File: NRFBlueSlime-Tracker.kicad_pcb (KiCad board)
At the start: 4 copper layers, 38 x 20 mm, 61 parts, among them J1 GT-USB-7010ASV, Q1 NTS2101PT1G, SW1 TS-1088-AR02016, U1 ICM-45686, U2 E73-2G4M08S1C, U3 LIS2MDL, U4 EA8103DHR, U5 TP4057-42-SOT26-R, X1 S2D32.768KB20F30T, Y1 Q13FC13500004

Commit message: sihashkdasfhjkads
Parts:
- removed D8: 1N5819WS, Diode_SMD:D_SOD-323
- removed Q1: NTS2101PT1G, Package_TO_SOT_SMD:SOT-323_SC-70
- added C18: 10u, Capacitor_SMD:C_0603_1608Metric, F.Cu at (52.6, 47.2)
- added C19: 100n, Capacitor_SMD:C_0402_1005Metric, F.Cu at (42.3, 37.2)
- added C20: 10u, Capacitor_SMD:C_0603_1608Metric, F.Cu at (56.6, 39.7)
- added C21: 100n, Capacitor_SMD:C_0402_1005Metric, F.Cu at (42.3, 39.2)
- added C22: 10u, Capacitor_SMD:C_0603_1608Metric, F.Cu at (56.6, 42.2)
- added C23: 100n, Capacitor_SMD:C_0402_1005Metric, F.Cu at (45.2, 29.3)
- added C24: 220n, Capacitor_SMD:C_0402_1005Metric, F.Cu at (45.2, 31.3)
- added C25: 220n, Capacitor_SMD:C_0402_1005Metric, F.Cu at (45.2, 33.3)
- added L2: 2.2u, Inductor_SMD:L_1210_3225Metric, F.Cu at (40.8, 42.3)
- added Y2: XL7EL89CKI-111YLC-32M, Crystal:Crystal_SMD_2016-4Pin_2.0x1.6mm, F.Cu at (43.8, 54.3)
- C1: value 10u -> 100p; footprint Capacitor_SMD:C_0603_1608Metric -> Capacitor_SMD:C_0402_1005Metric
- C10, C2: value 100n -> 1u; footprint Capacitor_SMD:C_0402_1005Metric -> Capacitor_SMD:C_0603_1608Metric
- C11, C6: value 220n -> 100n
- C12: value 10u -> 1u
- C13: value 10u -> 100n; footprint Capacitor_SMD:C_0603_1608Metric -> Capacitor_SMD:C_0402_1005Metric
- C14: value 1u -> 10u
- C16, C17: value 22p -> 4.7u; footprint Capacitor_SMD:C_0402_1005Metric -> Capacitor_SMD:C_0603_1608Metric
- C3: value 100n -> 100p
- C4: value 10u -> 15p; footprint Capacitor_SMD:C_0603_1608Metric -> Capacitor_SMD:C_0402_1005Metric
- C5: value 100n -> 15p
- C7: value 1u -> 0.8p; footprint Capacitor_SMD:C_0603_1608Metric -> Capacitor_SMD:C_0402_1005Metric
- C8: value 100n -> 6.8p
- C9: value 1u -> 6.8p; footprint Capacitor_SMD:C_0603_1608Metric -> Capacitor_SMD:C_0402_1005Metric
- L1: value 2.2u -> 4.7n; footprint Inductor_SMD:L_1210_3225Metric -> Inductor_SMD:L_0402_1005Metric
- R1, R2: value 5.1k -> 27
- R10: value 100k -> 51k
- R11: value 51k -> 10k; footprint Resistor_SMD:R_0603_1608Metric -> Resistor_SMD:R_0402_1005Metric
- R3: value 27 -> 1k
- R4: value 27 -> 5.1k
- R5: value 1k -> 5.1k
- R8: value 100k -> 10k; footprint Resistor_SMD:R_0603_1608Metric -> Resistor_SMD:R_0402_1005Metric
- R9: value 1k -> 100k; footprint Resistor_SMD:R_0402_1005Metric -> Resistor_SMD:R_0603_1608Metric
- TP1, TP2, TP3, TP4, TP5, TP6: moved to F.Cu
- U1: value ICM-45686 -> nRF52840; footprint 42688:PQFN50P300X250X97-14N -> Package_DFN_QFN:Nordic_AQFN-73-1EP_7x7mm_P0.5mm
- U2: value E73-2G4M08S1C -> EA8103DHR; footprint nrf:E73-2G4M08S1C_nobottom -> nrfslime:DFN-6_L1.5-W1.5-P0.50-BL-EP1.0
- U3: value LIS2MDL -> BQ24075RGT; footprint Package_LGA:LGA-12_2x2mm_P0.5mm -> Package_DFN_QFN:VQFN-16-1EP_3x3mm_P0.5mm_EP1.6x1.6mm
- U4: value EA8103DHR -> ICM-45686; footprint nrfslime:DFN-6_L1.5-W1.5-P0.50-BL-EP1.0 -> 42688:PQFN50P300X250X97-14N
- U5: value TP4057-42-SOT26-R -> LIS2MDL; footprint Package_TO_SOT_SMD:SOT-23-6 -> Package_LGA:LGA-12_2x2mm_P0.5mm
- Y1: value Q13FC13500004 -> XKXGI-SUA-32.768K
- moved U5 45.7 mm to (40.0, 54.5), turned to 0 degrees
- moved C11 40.6 mm to (42.3, 33.3)
- moved U4 40.3 mm to (40.7, 50.5)
- moved D4 38.1 mm to (48.0, 56.7), turned to 0 degrees
- moved C13 37.1 mm to (42.3, 35.2)
- moved D7 35.7 mm to (50.7, 54.3), turned to 0 degrees
- moved C6 34.7 mm to (39.4, 37.2), turned to 0 degrees
- moved D6 34.4 mm to (50.7, 52.0), turned to 0 degrees
- moved C15 33.7 mm to (52.6, 39.7), turned to 0 degrees
- moved C14 33.7 mm to (48.6, 47.2), turned to 0 degrees
- moved C4 33.4 mm to (39.4, 33.3)
- moved D5 33.1 mm to (50.7, 49.6), turned to 0 degrees
- moved C12 33.1 mm to (48.6, 44.7), turned to 0 degrees
- moved C1 33.0 mm to (39.4, 29.3), turned to 0 degrees
- moved LED3 32.2 mm to (54.1, 54.9), turned to 0 degrees
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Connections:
- C1 pad 1: +3V3 -> GND
- C1 pad 2: GND -> Net-(U1-DEC4)
- C10 pad 1: +3V3 -> VBUS
- C11 pad 1: KEY -> VBUS
- C12 pad 1: VDC -> +3V3
- C14 pad 1: GND -> VDC
- C14 pad 2: VBUS -> GND
- C15 pad 1: +BATT -> +3V3
- C16 pad 1: Net-(U2-XL1) -> GND
- C16 pad 2: Net-(C16-Pad2) -> VBUS
- C17 pad 1: Net-(U2-XL2) -> GND
- C17 pad 2: Net-(C17-Pad2) -> Net-(LED2-A)
- C2 pad 1: +3V3 -> GND
- C2 pad 2: GND -> Net-(U1-DEC4)
- C3 pad 1: +3V3 -> GND
- C3 pad 2: GND -> Net-(U1-DEC3)
- C4 pad 1: +3V3 -> Net-(U1-XL1/P0.00)
- C4 pad 2: GND -> Net-(C4-Pad2)
- C5 pad 1: +3V3 -> Net-(U1-XL2/P0.01)
- C5 pad 2: GND -> Net-(C5-Pad2)
- C6 pad 1: Net-(U3-C1) -> GND
- C6 pad 2: GND -> Net-(U1-DEC1)
- C7 pad 1: VBUS -> GND
- C7 pad 2: GND -> Net-(U1-ANT)
- C8 pad 1: VBUS -> Net-(C8-Pad1)
- C8 pad 2: GND -> Net-(U1-XC1)
- C9 pad 1: +3V3 -> Net-(C9-Pad1)
- C9 pad 2: GND -> Net-(U1-XC2)
- D6 pad 1: ~{RST} -> DOCK
- D7 pad 1: DOCK -> ~{RST}
- L1 pad 1: Net-(U4-SW) -> unconnected-(L1-Pad1)
- L1 pad 2: +3V3 -> Net-(U1-ANT)
- R1 pad 1: Net-(J1-CC1) -> DN
- R1 pad 2: GND -> Net-(U1-D-)
- R10 pad 1: BATLVL -> ~{ADC_EN}
- R10 pad 2: +BATT -> BATLVL
- R11 pad 1: ~{ADC_EN} -> Net-(U3-ISET)
- R11 pad 2: BATLVL -> GND
- R12 pad 1: GND -> Net-(U3-TS)
- R12 pad 2: Net-(U5-PROG) -> GND
- R2 pad 1: Net-(J1-CC2) -> DP
- R2 pad 2: GND -> Net-(U1-D+)
- R3 pad 1: DN -> Net-(LED1-A)
- R3 pad 2: Net-(U2-D-) -> +3V3
- R4 pad 1: DP -> Net-(J1-CC1)
- R4 pad 2: Net-(U2-D+) -> GND
- R5 pad 1: Net-(LED1-A) -> Net-(J1-CC2)
- R5 pad 2: +3V3 -> GND
- R6 pad 2: Net-(U4-FB) -> Net-(U2-FB)
- R7 pad 1: Net-(U4-FB) -> Net-(U2-FB)
- R8 pad 1: GND -> Net-(LED2-A)
- R8 pad 2: VBUS -> VDC
- R9 pad 1: Net-(LED2-A) -> BATLVL
- R9 pad 2: VBUS -> +BATT
- U2 pad 1: MOSI -> Net-(U2-SW)
- U2 pad 2: MISO -> VDC
- U2 pad 3: ~{ADC_EN} -> Net-(U2-FB)
- U2 pad 4: OSC_EN -> GND
- U2 pad 5: GND -> unconnected-(U2-NC-Pad5)
- U2 pad 6: ~{CS}_IMU -> VDC
- U2 pad 7: DOCK -> GND
- U3 pad 1: SCLK -> Net-(U3-TS)
- U3 pad 10: +3V3 -> VDC
- U3 pad 11: unconnected-(U3-NC-Pad11) -> VDC
- U3 pad 2: unconnected-(U3-NC-Pad2) -> +BATT
- U3 pad 3: ~{CS}_MAG -> +BATT
- U3 pad 4: MOSI -> GND
- U3 pad 5: Net-(U3-C1) -> GND
- U3 pad 6: GND -> VDC
- U3 pad 7: MISO -> Net-(LED2-K)
- U3 pad 9: +3V3 -> Net-(LED3-K)
- U4 pad 1: Net-(U4-SW) -> MISO
- U4 pad 2: VDC -> GND
- U4 pad 3: Net-(U4-FB) -> GND
- U4 pad 4: GND -> INT
- U4 pad 5: unconnected-(U4-NC-Pad5) -> +3V3
- U4 pad 6: VDC -> GND
- U5 pad 1: Net-(LED2-K) -> SCLK
- U5 pad 2: GND -> unconnected-(U5-NC-Pad2)
- U5 pad 3: +BATT -> ~{CS}_MAG
- U5 pad 4: VBUS -> MOSI
- U5 pad 5: Net-(LED3-K) -> Net-(U5-C1)
- U5 pad 6: Net-(U5-PROG) -> GND
- Y1 pad 1: Net-(C16-Pad2) -> Net-(C4-Pad2)
- Y1 pad 2: Net-(C17-Pad2) -> Net-(C5-Pad2)
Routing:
- net DOCK: track 41.8 -> 0.00 mm, vias 2 -> 0
- net VBUS: track 41.1 -> 0.00 mm, vias 4 -> 0
- net GND: track 39.8 -> 0.00 mm, vias 14 -> 0
- net BATLVL: track 35.2 -> 0.00 mm, vias 4 -> 0
- net ~{CS}_MAG: track 35.0 -> 0.00 mm, vias 2 -> 0
- net SWC: track 33.9 -> 0.00 mm, vias 2 -> 0
- net ~{RST}: track 31.7 -> 0.00 mm, vias 3 -> 0
- net MISO: track 30.5 -> 0.00 mm, vias 3 -> 0
- net ~{ADC_EN}: track 30.1 -> 0.00 mm, vias 2 -> 0
- net +3V3: track 26.7 -> 0.00 mm, vias 9 -> 0
- net MOSI: track 26.2 -> 0.00 mm, vias 3 -> 0
- net SWD: track 25.8 -> 0.00 mm, vias 2 -> 0
- net KEY: track 25.6 -> 0.00 mm, vias 3 -> 0
- net SCLK: track 24.1 -> 0.00 mm, vias 4 -> 0
- net ~{CS}_IMU: track 23.7 -> 0.00 mm, vias 3 -> 0
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- removed copper zone on In2.Cu, net +3V3
- removed copper zone on B.Cu, net GND
- removed copper zone on F.Cu, net GND
- removed copper zone on In1.Cu, net GND
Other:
- board outline removed
- board text removed: "+ -"

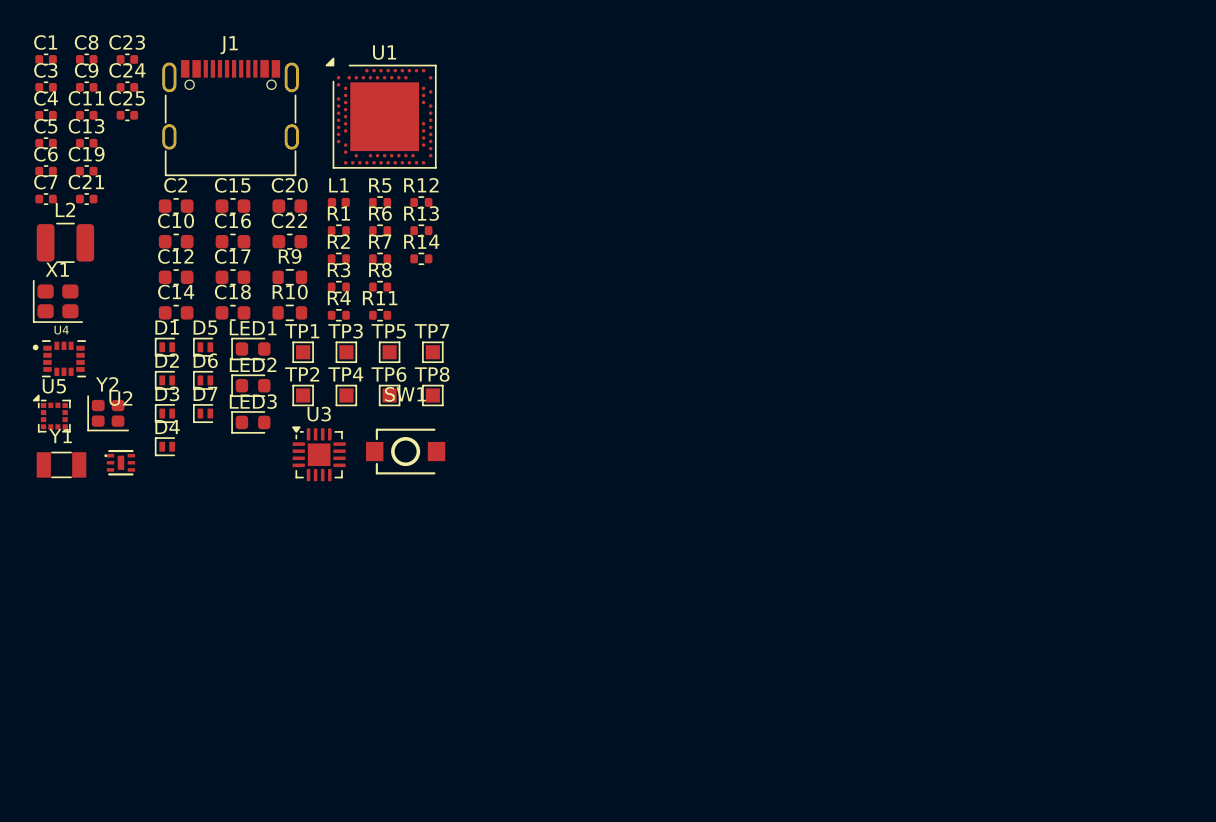
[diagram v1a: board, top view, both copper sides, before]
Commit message: place components
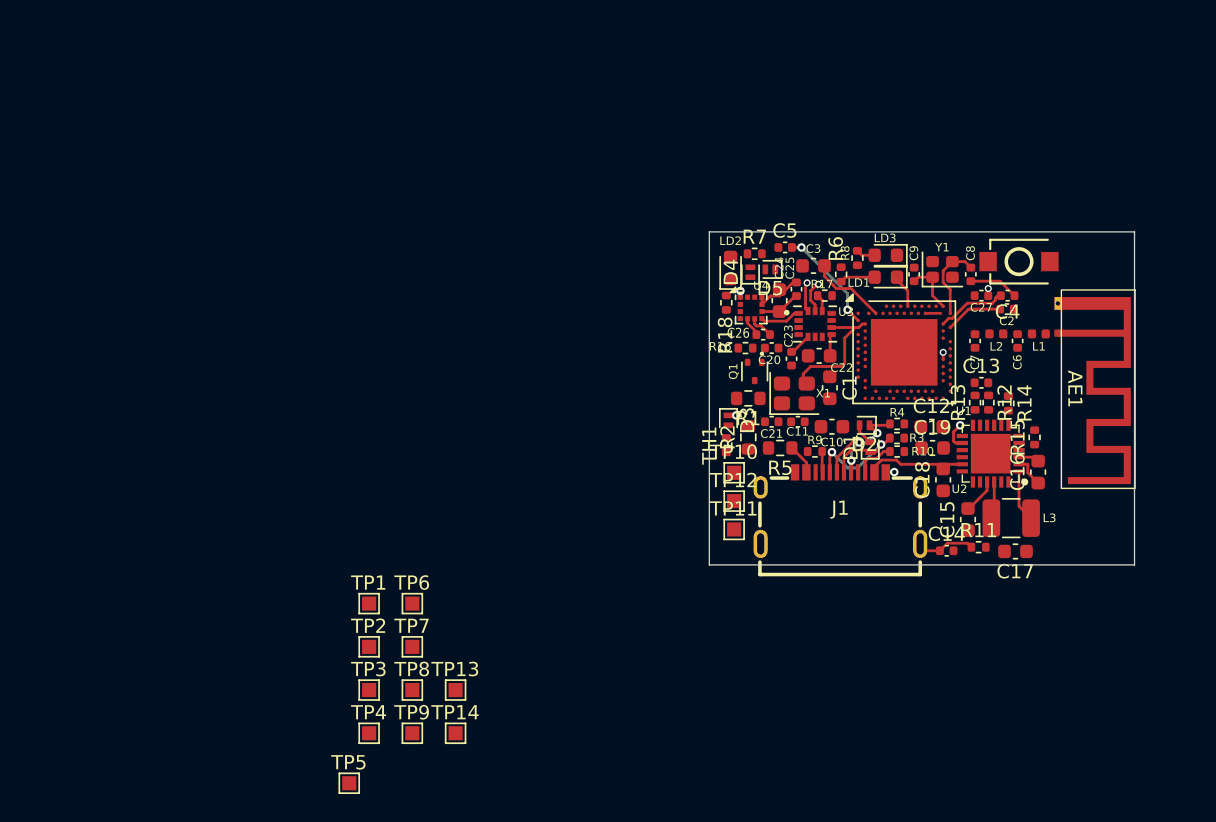
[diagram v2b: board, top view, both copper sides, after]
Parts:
- removed D6, D7: PESD5V0X1UB, Diode_SMD:D_SOD-882
- removed LED1: XL-1608UBC-04, LED_SMD:LED_0603_1608Metric
- removed LED2: XL-1608SURC-06, LED_SMD:LED_0603_1608Metric
- removed LED3: XL-1608UGC-06, LED_SMD:LED_0603_1608Metric
- removed U5: LIS2MDL, Package_LGA:LGA-12_2x2mm_P0.5mm
- removed Y2: XL7EL89CKI-111YLC-32M, Crystal:Crystal_SMD_2016-4Pin_2.0x1.6mm
- added AE1: Antenna_Shield, nrfslime:MIFA_BLE_ANT, F.Cu at (111.1, 48.6)
- added C26: 220n, Capacitor_SMD:C_0402_1005Metric, F.Cu at (90.0, 48.8)
- added C27: 220n, Capacitor_SMD:C_0402_1005Metric, F.Cu at (105.5, 46.0)
- added L3: 2.2u, Inductor_SMD:L_1210_3225Metric, F.Cu at (107.5, 61.7)
- added LD1: XL-1608UBC-04, LED_SMD:LED_0603_1608Metric, F.Cu at (98.7, 44.7)
- added LD2: XL-1608SURC-06, LED_SMD:LED_0603_1608Metric, F.Cu at (87.8, 44.0)
- added LD3: XL-1608UGC-06, LED_SMD:LED_0603_1608Metric, F.Cu at (98.7, 43.1)
- added Q1: YFW2301T, Package_TO_SOT_SMD:SOT-523, F.Cu at (89.5, 51.4)
- added R15: 470k, Resistor_SMD:R_0402_1005Metric, F.Cu at (109.2, 56.0)
- added R16: 470k, Resistor_SMD:R_0402_1005Metric, F.Cu at (88.8, 49.7)
- added R17: 470k, Resistor_SMD:R_0402_1005Metric, F.Cu at (94.4, 46.0)
- added R18: 470k, Resistor_SMD:R_0402_1005Metric, F.Cu at (87.5, 46.5)
- added TH1: HNTC0402-103F3380FB, Resistor_SMD:R_0402_1005Metric, F.Cu at (87.5, 56.5)
- added TP10: TestPoint, TestPoint:TestPoint_Pad_1.0x1.0mm, F.Cu at (88.0, 58.5)
- added TP11: TestPoint, TestPoint:TestPoint_Pad_1.0x1.0mm, F.Cu at (88.0, 62.5)
- added TP12: TestPoint, TestPoint:TestPoint_Pad_1.0x1.0mm, F.Cu at (88.0, 60.5)
- added TP13: TestPoint, TestPoint:TestPoint_Pad_1.0x1.0mm, F.Cu at (68.3, 73.8)
- added TP14: TestPoint, TestPoint:TestPoint_Pad_1.0x1.0mm, F.Cu at (68.3, 76.9)
- added TP9: TestPoint, TestPoint:TestPoint_Pad_1.0x1.0mm, F.Cu at (65.3, 76.9)
- C1: value 100p -> 4.7u; footprint Capacitor_SMD:C_0402_1005Metric -> Capacitor_SMD:C_0603_1608Metric
- C10, C12: value 1u -> 4.7u
- C14: value 10u -> 100n; footprint Capacitor_SMD:C_0603_1608Metric -> Capacitor_SMD:C_0402_1005Metric
- C16, C17: value 4.7u -> 10u
- C18: value 10u -> 2.2u
- C19: value 100n -> 1u; footprint Capacitor_SMD:C_0402_1005Metric -> Capacitor_SMD:C_0603_1608Metric
- C2: value 1u -> 100p; footprint Capacitor_SMD:C_0603_1608Metric -> Capacitor_SMD:C_0402_1005Metric
- C20: value 10u -> 1n; footprint Capacitor_SMD:C_0603_1608Metric -> Capacitor_SMD:C_0402_1005Metric
- C24: value 220n -> 10u; footprint Capacitor_SMD:C_0402_1005Metric -> Capacitor_SMD:C_0603_1608Metric
- C25: value 220n -> 100n
- C3: value 100p -> 1u; footprint Capacitor_SMD:C_0402_1005Metric -> Capacitor_SMD:C_0603_1608Metric
- C4: value 15p -> 100p
- C5: value 15p -> 100n
- C6: value 100n -> 1.2p
- C7: value 0.8p -> 1p
- J1: value GT-USB-7010ASV -> HC-TYPE-C-16P-C10B; footprint Connector_USB:USB_C_Receptacle_G-Switch_GT-USB-7010ASV -> nrfslime:USB-C-SMD_HC-TYPE-C-16P-C10B
- L1: value 4.7n -> 2.2n
- L2: value 2.2u -> 4.7n; footprint Inductor_SMD:L_1210_3225Metric -> Inductor_SMD:L_0402_1005Metric
- R1, R2: value 27 -> 0; footprint Resistor_SMD:R_0402_1005Metric -> Resistor_SMD:R_0603_1608Metric
- R10: value 51k -> 5.1k; footprint Resistor_SMD:R_0603_1608Metric -> Resistor_SMD:R_0402_1005Metric
- R11: value 10k -> 1M
- R12: value 10k -> 100k
- R13: value 100k -> 4.7k
- R14: value 100k -> 470k
- R3: value 1k -> 27
- R4: value 5.1k -> 27
- R5: value 5.1k -> 1; footprint Resistor_SMD:R_0402_1005Metric -> Resistor_SMD:R_0603_1608Metric
- R6: value 965k -> 510
- R7: value 499k -> 510
- R8: value 10k -> 510
- R9: value 100k -> 5.1k; footprint Resistor_SMD:R_0603_1608Metric -> Resistor_SMD:R_0402_1005Metric
- U2: value EA8103DHR -> NPM1100-QDAA-R; footprint nrfslime:DFN-6_L1.5-W1.5-P0.50-BL-EP1.0 -> npm1100-q:QFN50P400X400X90-25N-D
- U3: value BQ24075RGT -> ICM-45686; footprint Package_DFN_QFN:VQFN-16-1EP_3x3mm_P0.5mm_EP1.6x1.6mm -> 42688:PQFN50P300X250X97-14N
- U4: value ICM-45686 -> LIS2MDL; footprint 42688:PQFN50P300X250X97-14N -> Package_LGA:LGA-12_2x2mm_P0.5mm
- X1: value S2D32.768KB20F30T -> SX2M32.768KM20F30TNN
- Y1: value XKXGI-SUA-32.768K -> XL7EL89CKI-111YLC-32M; footprint Crystal:Crystal_SMD_3215-2Pin_3.2x1.5mm -> Crystal:Crystal_SMD_2016-4Pin_2.0x1.6mm
- moved C6 69.6 mm to (108.0, 49.2), turned to 90 degrees
- moved C4 69.0 mm to (107.3, 46.0), turned to 180 degrees
- moved C7 66.3 mm to (105.0, 49.2), turned to 90 degrees
- moved L2 66.0 mm to (106.5, 48.7), turned to 180 degrees
- moved C13 65.4 mm to (105.5, 52.1)
- moved C8 64.2 mm to (104.7, 44.5), turned to 90 degrees
- moved Y1 63.7 mm to (102.7, 44.1)
- moved C19 62.8 mm to (102.0, 56.8)
- moved U2 61.4 mm to (106.1, 57.1), turned to 180 degrees
- moved C1 60.0 mm to (94.8, 52.5), turned to -90 degrees
- moved C9 59.9 mm to (100.7, 44.5), turned to -90 degrees
- moved C16 59.1 mm to (109.5, 58.5), turned to 90 degrees
- moved C2 59.1 mm to (107.2, 47.0), turned to 180 degrees
- moved C17 58.5 mm to (107.8, 64.0), turned to 180 degrees
- moved C14 56.9 mm to (103.0, 64.0)
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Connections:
- C1 pad 2: Net-(U1-DEC4) -> Net-(U1-DECUSB)
- C10 pad 1: VBUS -> VBUS_NRF
- C11 pad 1: VBUS -> VBUS_NRF
- C12 pad 1: +3V3 -> +1V8
- C13 pad 1: +3V3 -> +1V8
- C14 pad 1: VDC -> Net-(J1-SHIELD)
- C15 pad 1: +3V3 -> GND
- C15 pad 2: GND -> Net-(U2-DEC)
- C16 pad 2: VBUS -> VSYS
- C17 pad 1: GND -> +1V8
- C17 pad 2: Net-(LED2-A) -> GND
- C18 pad 2: +BATT -> VBUS
- C19 pad 1: +3V3 -> GND
- C19 pad 2: GND -> +BATT
- C20 pad 1: +3V3 -> ~{OSC_EN}
- C21 pad 1: +3V3 -> Net-(Q1-D)
- C22 pad 1: +3V3 -> +1V8
- C23 pad 1: +3V3 -> +1V8
- C24 pad 1: Net-(U5-C1) -> +1V8
- C25 pad 1: KEY -> +1V8
- C3 pad 2: Net-(U1-DEC3) -> Net-(U1-DEC4)
- C4 pad 1: Net-(U1-XL1/P0.00) -> GND
- C4 pad 2: Net-(C4-Pad2) -> Net-(U1-DEC3)
- C5 pad 1: Net-(U1-XL2/P0.01) -> GND
- C5 pad 2: Net-(C5-Pad2) -> Net-(U1-DEC1)
- C6 pad 2: Net-(U1-DEC1) -> Net-(C6-Pad2)
- C8 pad 1: Net-(C8-Pad1) -> GND
- C9 pad 1: Net-(C9-Pad1) -> GND
- D1 pad 1: DN -> DNX
- D2 pad 1: DP -> DPX
- D4 pad 1: SWD -> ~{RST}
- D5 pad 1: SWC -> DOCK
- J1 pad A6: DP -> DPX
- J1 pad A7: DN -> DNX
- J1 pad B6: DP -> DPX
- J1 pad B7: DN -> DNX
- J1 pad S1: GND -> Net-(J1-SHIELD)
- L1 pad 1: unconnected-(L1-Pad1) -> Net-(AE1-A)
- L1 pad 2: Net-(U1-ANT) -> Net-(C6-Pad2)
- L2 pad 1: Net-(U2-SW) -> Net-(C6-Pad2)
- L2 pad 2: +3V3 -> Net-(U1-ANT)
- R1 pad 1: DN -> Net-(U1-VDDH)
- R1 pad 2: Net-(U1-D-) -> +1V8
- R10 pad 1: ~{ADC_EN} -> Net-(J1-CC2)
- R10 pad 2: BATLVL -> GND
- R11 pad 1: Net-(U3-ISET) -> Net-(J1-SHIELD)
- R12 pad 1: Net-(U3-TS) -> +BATT
- R12 pad 2: GND -> Net-(U2-SHPHLD)
- R13 pad 1: ~{CS}_IMU -> Net-(U2-ICHG)
- R13 pad 2: +3V3 -> GND
- R14 pad 1: ~{CS}_MAG -> GND
- R14 pad 2: +3V3 -> NPM_MODE
- R2 pad 1: DP -> VBUS_NRF
- R2 pad 2: Net-(U1-D+) -> Net-(U1-VDDH)
- R3 pad 1: Net-(LED1-A) -> DNX
- R3 pad 2: +3V3 -> DN
- R4 pad 1: Net-(J1-CC1) -> DP
- R4 pad 2: GND -> DPX
- R5 pad 1: Net-(J1-CC2) -> VBUS
- R5 pad 2: GND -> VBUS_NRF
- R6 pad 1: +3V3 -> Net-(LD1-A)
- R6 pad 2: Net-(U2-FB) -> +1V8
- R7 pad 1: Net-(U2-FB) -> Net-(LD2-A)
- R7 pad 2: GND -> +1V8
- R8 pad 1: Net-(LED2-A) -> Net-(LD3-A)
- R8 pad 2: VDC -> +1V8
- R9 pad 1: BATLVL -> Net-(J1-CC1)
- R9 pad 2: +BATT -> GND
- TP1 pad 1: VBUS -> SWD
- TP2 pad 1: SWD -> SHPACT
- TP4 pad 1: ~{RST} -> +1V8
- TP6 pad 1: DOCK -> VBUS
- TP7 pad 1: +BATT -> DP
- TP8 pad 1: GND -> DN
- U1 pad A12: BATLVL -> unconnected-(U1-AIN0/P0.02-PadA12)
- U1 pad A14: LED -> ~{LED_STAT}
- U1 pad A16: OSC_EN -> ~{OSC_EN}
- U1 pad A22: +3V3 -> +1V8
- U1 pad A8: unconnected-(U1-AIN7/P0.31-PadA8) -> ~{ADC_EN}
- U1 pad AC11: INT -> unconnected-(U1-P0.16-PadAC11)
- U1 pad AC13: BATLVL -> ~{RST}
- U1 pad AC21: MOSI -> SCLK
- U1 pad AC5: unconnected-(U1-DECUSB-PadAC5) -> Net-(U1-DECUSB)
- U1 pad AD10: unconnected-(U1-P0.15-PadAD10) -> INT
- U1 pad AD14: +3V3 -> +1V8
- U1 pad AD2: VBUS -> VBUS_NRF
- U1 pad AD23: +3V3 -> +1V8
- U1 pad AD4: Net-(U1-D-) -> DN
- U1 pad AD6: Net-(U1-D+) -> DP
- U1 pad B1: +3V3 -> +1V8
- U1 pad B15: ~{ADC_EN} -> unconnected-(U1-P1.14-PadB15)
- U1 pad D2: Net-(U1-XL1/P0.00) -> CLK
- U1 pad F2: Net-(U1-XL2/P0.01) -> GND
- U1 pad L1: unconnected-(U1-P0.06-PadL1) -> ~{LED_CHG}
- U1 pad N1: unconnected-(U1-P0.08-PadN1) -> ~{LED_ERR}
- U1 pad P23: unconnected-(U1-P1.07-PadP23) -> NPM_MODE
- U1 pad R24: unconnected-(U1-P1.06-PadR24) -> NPM_ISET
- U1 pad U24: unconnected-(U1-P1.04-PadU24) -> NPM_~{ERR}
- U1 pad W1: +3V3 -> +1V8
- U1 pad W24: unconnected-(U1-P1.02-PadW24) -> NPM_~{CHG}
- U1 pad Y2: +3V3 -> Net-(U1-VDDH)
- U2 pad 1: Net-(U2-SW) -> +1V8
- U2 pad 2: VDC -> GND
- U2 pad 3: Net-(U2-FB) -> VSYS
- U2 pad 5: unconnected-(U2-NC-Pad5) -> NPM_ISET
- U2 pad 6: VDC -> SHPACT
- U2 pad 7: GND -> NPM_MODE
- U3 pad 1: Net-(U3-TS) -> MISO
- U3 pad 10: VDC -> GND
- U3 pad 11: VDC -> GND
- U3 pad 12: unconnected-(U3-ILIM-Pad12) -> ~{CS}_IMU
- U3 pad 13: VBUS -> SCLK
- U3 pad 14: unconnected-(U3-TMR-Pad14) -> MOSI
- U3 pad 2: +BATT -> GND
- U3 pad 3: +BATT -> GND
- U3 pad 4: GND -> INT
- U3 pad 5: GND -> +1V8
- U3 pad 6: VDC -> GND
- U3 pad 7: Net-(LED2-K) -> GND
- U3 pad 8: GND -> +1V8
- U3 pad 9: Net-(LED3-K) -> CLK
- U4 pad 1: MISO -> SCLK
- U4 pad 10: GND -> +1V8
- U4 pad 11: GND -> unconnected-(U4-NC-Pad11)
- U4 pad 12: ~{CS}_IMU -> unconnected-(U4-NC-Pad12)
- U4 pad 2: GND -> unconnected-(U4-NC-Pad2)
- U4 pad 3: GND -> ~{CS}_MAG
- U4 pad 4: INT -> MOSI
- U4 pad 5: +3V3 -> Net-(U4-C1)
- U4 pad 7: GND -> MISO
- U4 pad 8: +3V3 -> GND
- U4 pad 9: CLK -> +1V8
- X1 pad 1: OSC_EN -> Net-(Q1-D)
- X1 pad 4: +3V3 -> Net-(Q1-D)
- Y1 pad 1: Net-(C4-Pad2) -> Net-(U1-XC2)
- Y1 pad 2: Net-(C5-Pad2) -> GND
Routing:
- net GND: track 0.00 -> 12.7 mm, vias 0 -> 1
- net DNX: track 0.00 -> 11.1 mm, vias 0 -> 2
- net +1V8: track 0.00 -> 10.4 mm
- net Net-(U1-DEC4): track 0.00 -> 9.52 mm
- net CLK: track 0.00 -> 9.46 mm
- net DPX: track 0.00 -> 9.20 mm, vias 0 -> 3
- net VBUS: track 0.00 -> 8.88 mm, vias 0 -> 1
- net Net-(U1-DEC1): track 0.00 -> 7.48 mm, vias 0 -> 2
- net Net-(U1-XC1): track 0.00 -> 5.60 mm
- net Net-(U1-DEC3): track 0.00 -> 4.99 mm
- net Net-(J1-SHIELD): track 0.00 -> 4.15 mm
- net Net-(U1-XC2): track 0.00 -> 3.78 mm
- net Net-(U2-SW): track 0.00 -> 2.92 mm
- net MISO: track 0.00 -> 2.89 mm
- net Net-(J1-CC2): track 0.00 -> 2.80 mm
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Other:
- board outline added: 30 x 23.5 mm

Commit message: sync
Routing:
- net Net-(Q1-D): track 0.00 -> 5.21 mm
- net +1V8: track 10.4 -> 14.2 mm
- net Net-(U1-VDDH): track 0.00 -> 2.27 mm
- net ~{OSC_EN}: track 0.00 -> 1.96 mm
- net Net-(LD2-A): track 0.00 -> 1.28 mm
- net ~{CS}_MAG: track 0.00 -> 1.03 mm
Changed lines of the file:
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@@
+	)
+	(segment
+		(start 87.5625 47.1225)
+		(end 88.4375 47.1225)
+		(width 0.2)
+		(layer "F.Cu")
+		(net 21)
+	)
+	(segment
+		(start 87.45 47.01)
+		(end 87.5625 47.1225)
+		(width 0.2)
+		(layer "F.Cu")
+		(net 21)
 	)
 	(segment
@@
 	)
 	(segment
+		(start 92.4 45.07)
+		(end 91.705 45.07)
+		(width 0.2)
+		(layer "F.Cu")
+		(net 33)
+	)
+	(segment
 		(start 92.1575 49.97)
 		(end 93.2125 48.915)
@@
 	)
 	(segment
+		(start 96.57 43.99)
+		(end 96.7 43.86)
+		(width 0.2)
+		(layer "F.Cu")
+		(net 33)
+	)
+	(segment
 		(start 92.05 49.97)
 		(end 92.1575 49.97)
@@
 	)
 	(segment
+		(start 91.705 45.07)
+		(end 91.2 45.575)
+		(width 0.2)
+		(layer "F.Cu")
+		(net 33)
+	)
+	(segment
 		(start 89.9625 46.1225)
 		(end 89.9625 46.6225)
@@
 	)
 	(segment
-		(start 92.4 45.07)
-		(end 92.155 45.07)
-		(width 0.2)
-		(layer "F.Cu")
-		(net 33)
-	)
-	(segment
-		(start 92.155 45.07)
-		(end 91.2 46.025)
-		(width 0.2)
-		(layer "F.Cu")
-		(net 33)
-	)
-	(segment
 		(start 94.775 48.8525)
 		(end 94.8775 48.75)
@@
 	)
 	(segment
-		(start 90.56 46.025)
-		(end 89.9625 46.6225)
-		(width 0.2)
-		(layer "F.Cu")
-		(net 33)
-	)
-	(segment
-		(start 91.2 46.025)
-		(end 90.56 46.025)
+		(start 88.175 53.25)
+		(end 88.175 51.48)
+		(width 0.2)
+		(layer "F.Cu")
+		(net 33)
+	)
+	(segment
+		(start 95.55 43.99)
+		(end 96.57 43.99)
+		(width 0.2)
+		(layer "F.Cu")
+		(net 33)
+	)
+	(segment
+		(start 91.01 45.575)
+		(end 90.4625 46.1225)
+		(width 0.2)
+		(layer "F.Cu")
+		(net 33)
+	)
+	(segment
+		(start 91.2 45.575)
+		(end 91.01 45.575)
+		(width 0.2)
+		(layer "F.Cu")
+		(net 33)
+	)
+	(segment
+		(start 90.4625 46.1225)
+		(end 89.9625 46.1225)
 		(width 0.2)
 		(layer "F.Cu")
@@
 	)
 	(segment
+		(start 88.175 51.48)
+		(end 88.95 50.705)
+		(width 0.2)
+		(layer "F.Cu")
+		(net 33)
+	)
+	(segment
 		(start 101.61 64)
 		(end 101.13 63.52)
@@
 	)
 	(segment
+		(start 89.95 49.92)
+		(end 90.17 49.7)
+		(width 0.2)
+		(layer "F.Cu")
+		(net 38)
+	)
+	(segment
+		(start 89.95 50.705)
+		(end 89.95 49.92)
+		(width 0.2)
+		(layer "F.Cu")
+		(net 38)
+	)
+	(segment
+		(start 89.31 49.7)
+		(end 90.17 49.7)
+		(width 0.2)
+		(layer "F.Cu")
+		(net 38)
+	)
+	(segment
+		(start 91.375 52.2)
+		(end 89.655 52.2)
+		(width 0.2)
+		(layer "F.Cu")
+		(net 42)
+	)
+	(segment
+		(start 90.17 54.805)
+		(end 91.375 53.6)
+		(width 0.2)
+		(layer "F.Cu")
+		(net 42)
+	)
+	(segment
+		(start 90.17 54.9)
+		(end 90.17 54.805)
+		(width 0.2)
+		(layer "F.Cu")
+		(net 42)
+	)
+	(segment
+		(start 91.375 53.6)
+		(end 91.375 52.2)
+		(width 0.2)
+		(layer "F.Cu")
+		(net 42)
+	)
+	(segment
+		(start 89.655 52.2)
+		(end 89.45 51.995)
+		(width 0.2)
+		(layer "F.Cu")
+		(net 42)
+	)
+	(segment
 		(start 89.651822 48.65)
 		(end 88.95 47.948178)
@@
 	)
 	(segment
+		(start 88.7275 43.2625)
+		(end 88.94 43.05)
+		(width 0.2)
+		(layer "F.Cu")
+		(net 72)
+	)
+	(segment
+		(start 87.75 43.2625)
+		(end 88.7275 43.2625)
+		(width 0.2)
+		(layer "F.Cu")
+		(net 72)
+	)
+	(segment
 		(start 97.9125 43.15)
 		(end 97.01 43.15)
@@
 	)
 	(segment
+		(start 89 54.075)
+		(end 89.825 53.25)
+		(width 0.2)
+		(layer "F.Cu")
+		(net 75)
+	)
+	(segment
+		(start 89 55.175)
+		(end 89 54.075)
+		(width 0.2)
+		(layer "F.Cu")
+		(net 75)
+	)
+	(segment

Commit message: sync
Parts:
- TP1, TP13, TP14, TP2, TP3, TP4, TP5, TP6, TP7, TP8, TP9: moved to B.Cu
- moved TP5 57.4 mm to (106.0, 45.0), turned to 180 degrees
- moved TP9 50.1 mm to (104.0, 45.0), turned to 180 degrees
- moved TP13 48.7 mm to (106.0, 43.0), turned to 180 degrees
- moved TP4 47.3 mm to (106.0, 59.0), turned to 180 degrees
- moved TP3 46.7 mm to (104.0, 53.0), turned to 180 degrees
- moved TP2 46.5 mm to (106.0, 55.0), turned to 180 degrees
- moved TP1 43.7 mm to (104.0, 55.0), turned to 180 degrees
- moved TP8 42.7 mm to (106.0, 61.0), turned to 180 degrees
- moved TP14 42.6 mm to (106.0, 57.0), turned to 180 degrees
- moved TP6 40.2 mm to (104.0, 57.0), turned to 180 degrees
- moved TP7 39.9 mm to (104.0, 61.0), turned to 180 degrees
- moved D4 16.9 mm to (106.0, 46.6), turned to 180 degrees
- moved TH1 15.2 mm to (101.9, 61.3), turned to -90 degrees
- moved TP10 8.44 mm to (79.7, 57.0)
- moved TP12 8.37 mm to (79.7, 59.5)
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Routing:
- net MOSI: track 2.10 -> 29.0 mm, vias 1 -> 3
- net ~{CS}_IMU: track 1.22 -> 26.8 mm, vias 0 -> 2
- net INT: track 0.00 -> 23.9 mm, vias 0 -> 2
- net SCLK: track 2.75 -> 24.6 mm, vias 2 -> 3
- net GND: track 12.7 -> 34.4 mm, vias 1 -> 17
- net VBUS: track 8.88 -> 30.5 mm, vias 1 -> 5
- net ~{LED_ERR}: track 0.00 -> 21.2 mm, vias 0 -> 4
- net ~{CS}_MAG: track 1.03 -> 21.1 mm, vias 0 -> 2
- net MISO: track 2.89 -> 22.1 mm, vias 0 -> 2
- net DN: track 0.00 -> 17.8 mm, vias 0 -> 3
- net ~{RST}: track 0.00 -> 17.8 mm, vias 0 -> 2
- net ~{LED_CHG}: track 0.00 -> 16.5 mm, vias 0 -> 2
- net NPM_~{ERR}: track 0.00 -> 16.4 mm, vias 0 -> 2
- net +1V8: track 14.2 -> 30.4 mm, vias 0 -> 11
- net VSYS: track 1.46 -> 17.5 mm, vias 0 -> 3
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- added copper zone on In1.Cu, net +1V8
- added copper zone on B.Cu, net GND
- added copper zone on F.Cu, net GND
- added copper zone on In2.Cu, net GND
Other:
- outline, holes or cut-outs redrawn

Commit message: done pcb
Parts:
- moved TP10 20.7 mm to (99.5, 63.0)
- moved TP11 20.0 mm to (99.5, 59.0)
- moved TP12 19.9 mm to (99.5, 61.0)
- moved R17 0.18 mm to (93.2, 45.4)
- moved AE1 0.08 mm to (109.8, 48.2)
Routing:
- net GND: track 34.4 -> 61.4 mm, vias 17 -> 32
- net Net-(J1-SHIELD): track 4.15 -> 27.7 mm
- net NTC: track 1.99 -> 13.1 mm, vias 1 -> 3
- net Net-(U1-DEC4): track 8.97 -> 17.8 mm, vias 0 -> 2
- net SCLK: track 24.6 -> 31.2 mm
- net +1V8: track 30.4 -> 34.9 mm, vias 11 -> 12
- net +BATT: track 10.1 -> 14.0 mm
- net MOSI: track 29.0 -> 26.2 mm
- net Net-(U1-ANT): track 1.02 -> 3.25 mm
- net Net-(C6-Pad2): track 0.00 -> 2.03 mm
- net Net-(LD1-A): track 0.00 -> 1.52 mm
- net ~{CS}_IMU: track 26.8 -> 25.4 mm
- net VSYS: track 17.5 -> 16.3 mm
- net SWD: track 5.28 -> 4.17 mm
- net Net-(U1-DEC1): track 7.48 -> 8.40 mm
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- added copper zone on In2.Cu, net +1V8
- added copper zone on In1.Cu, net GND
- removed copper zone on In1.Cu, net +1V8
- removed copper zone on In2.Cu, net GND
